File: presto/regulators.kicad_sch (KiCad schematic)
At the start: 1 part

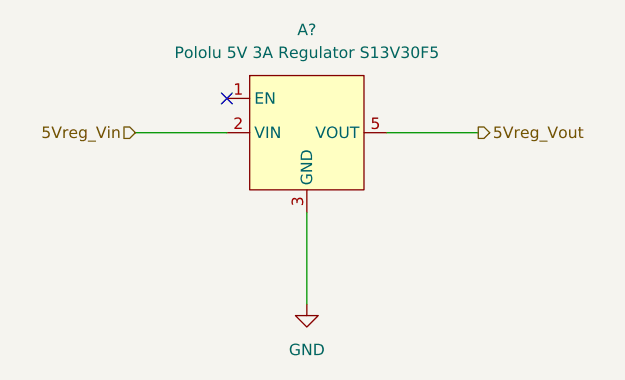
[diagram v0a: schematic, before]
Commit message: Presto PCB edited with schematic, components placed, wiring in progress
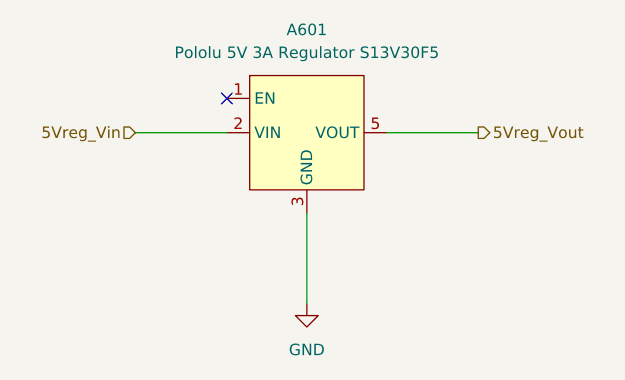
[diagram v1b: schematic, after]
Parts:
- gave numbers to parts that had none: 1
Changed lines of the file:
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@@
 		(dnp no)
 		(fields_autoplaced yes)
-		(property "Reference" "#PWR?"
+		(property "Reference" "#PWR0601"
 			(at 66.04 66.04 0)
 			(effects
@@
 			(project "presto"
 				(path "/0fac30c0-3f82-4ab4-8888-b9c60b2e0ca9/f58c1695-506e-4133-a5b9-df6f2b530f90"
-					(reference "#PWR?")
+					(reference "#PWR0601")
 					(unit 1)
 				)
@@
 		(dnp no)
 		(fields_autoplaced yes)
-		(property "Reference" "A?"
+		(property "Reference" "A601"
 			(at 66.04 29.21 0)
 			(effects
@@
 			(project "presto"
 				(path "/0fac30c0-3f82-4ab4-8888-b9c60b2e0ca9/f58c1695-506e-4133-a5b9-df6f2b530f90"
-					(reference "A?")
+					(reference "A601")
 					(unit 1)
 				)
